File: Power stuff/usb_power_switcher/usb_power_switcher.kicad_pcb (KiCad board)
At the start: 2 copper layers, 36.2 x 17.8 mm, 18 parts, among them J1 IN, J2 Conn_01x04, J3 OUT, J4 D+, J5 D-, J6 USB_OTG, Q1 Q_NPN_BEC, Q2 Q_PMOS_GSD

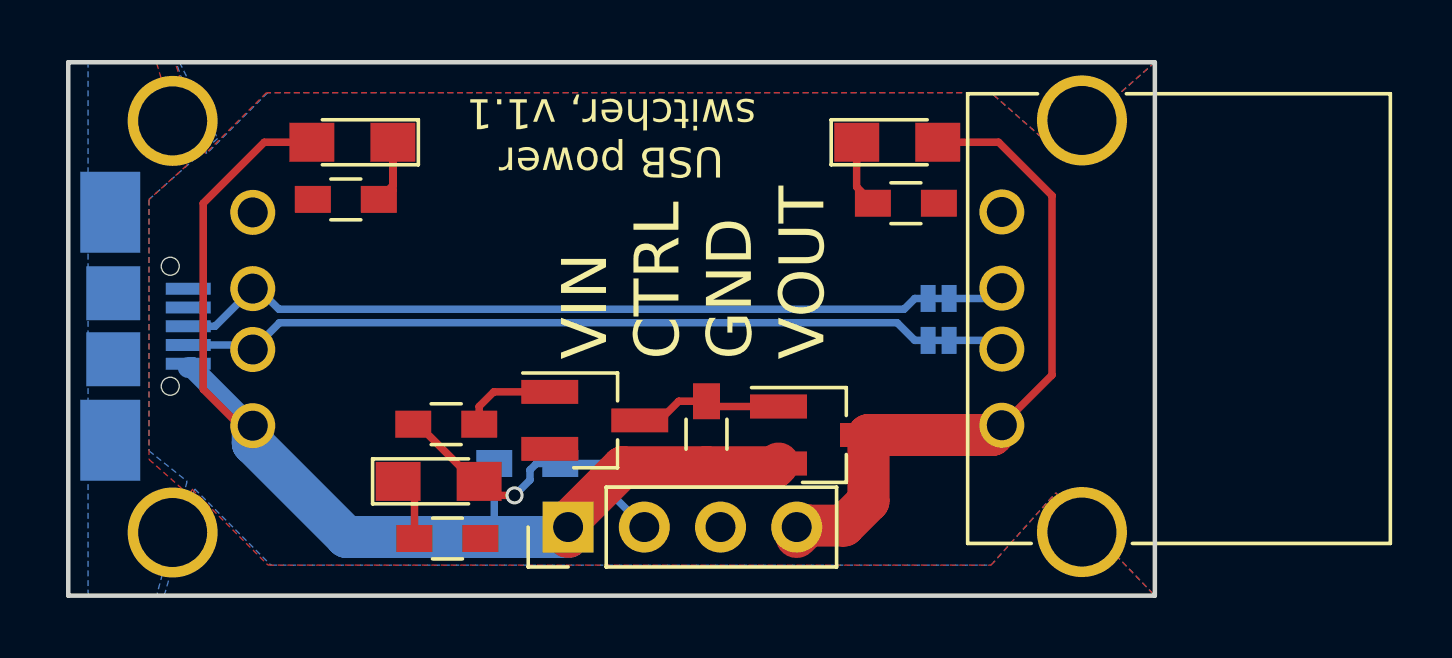
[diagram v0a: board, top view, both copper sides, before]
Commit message: Moving the MicroUSB socket to the top layer so that the board is easier to assemble, rearranging silkscreen a bit
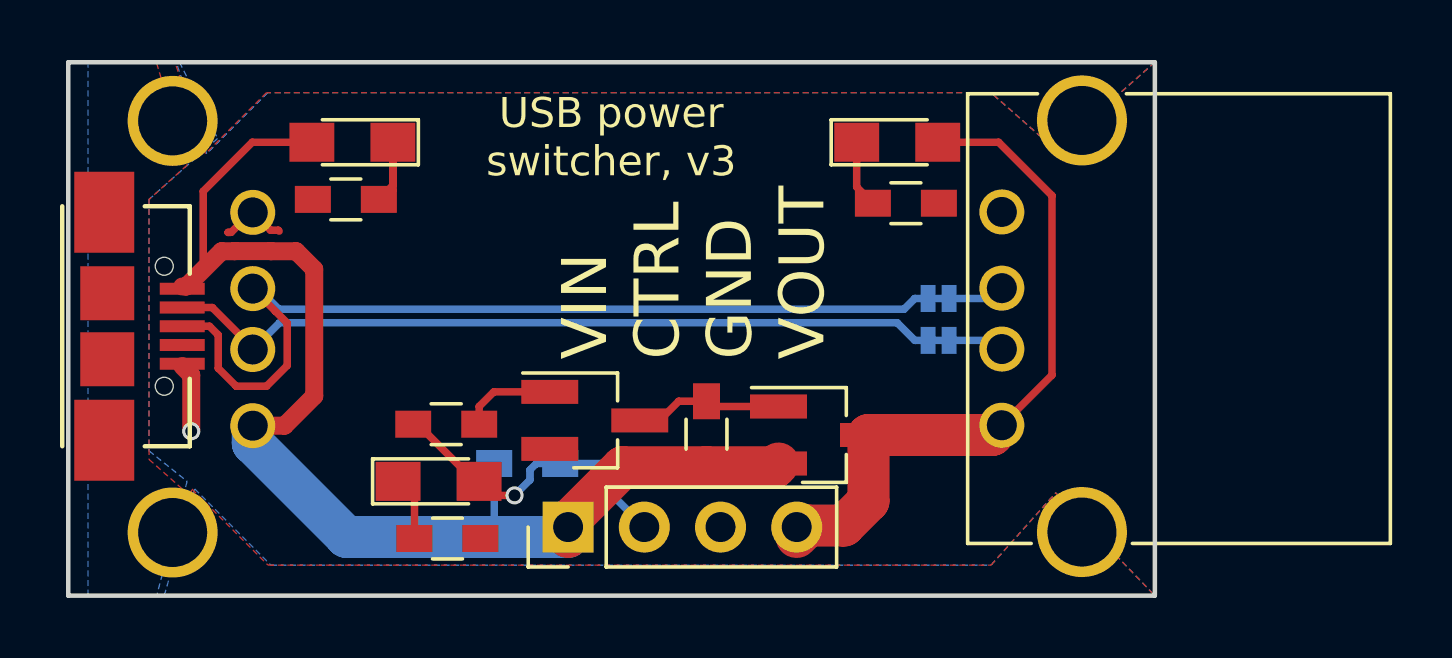
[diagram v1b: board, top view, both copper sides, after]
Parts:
- J6: moved to F.Cu
- moved J6 0.20 mm to (127.6, 97.7), turned to 90 degrees
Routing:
- net D+: track 28.4 -> 34.0 mm
- net GND: track 0.00 -> 4.54 mm, vias 0 -> 1
- net +5V: track 39.6 -> 43.9 mm
- net D-: track 27.9 -> 28.9 mm
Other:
- board text added: "USB power switcher, v3"
- board text removed: "USB power switcher, v1.1"

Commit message: Reloading the USB power switcher project files
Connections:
- J6 pad 4: (no net) -> Net-(J6-Pad4)
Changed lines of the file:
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@@
     (zones 0)
     (modules 18)
-    (nets 13)
+    (nets 14)
   )
   (page A4)
@@
   )
   (setup
-    (last_trace_width 0.6)
+    (last_trace_width 0.25)
     (user_trace_width 0.5)
     (user_trace_width 0.6)
@@
   (net 11 "Net-(D3-Pad1)")
   (net 12 "Net-(Q1-Pad3)")
+  (net 13 "Net-(J6-Pad4)")
   (net_class Default "This is the default net class."
     (clearance 0.2)
@@
     (add_net "Net-(D2-Pad1)")
     (add_net "Net-(D3-Pad1)")
+    (add_net "Net-(J6-Pad4)")
     (add_net "Net-(Q1-Pad1)")
     (add_net "Net-(Q1-Pad3)")
@@
     (pad 3 smd rect (at 0 0 90) (size 0.4 1.5) (layers F.Cu F.Paste F.Mask)
       (net 2 D+))
-    (pad 4 smd rect (at -0.625 0 90) (size 0.4 1.5) (layers F.Cu F.Paste F.Mask))
+    (pad 4 smd rect (at -0.625 0 90) (size 0.4 1.5) (layers F.Cu F.Paste F.Mask)
+      (net 13 "Net-(J6-Pad4)"))
     (pad 5 smd rect (at -1.25 0 90) (size 0.4 1.5) (layers F.Cu F.Paste F.Mask)
       (net 1 GND))

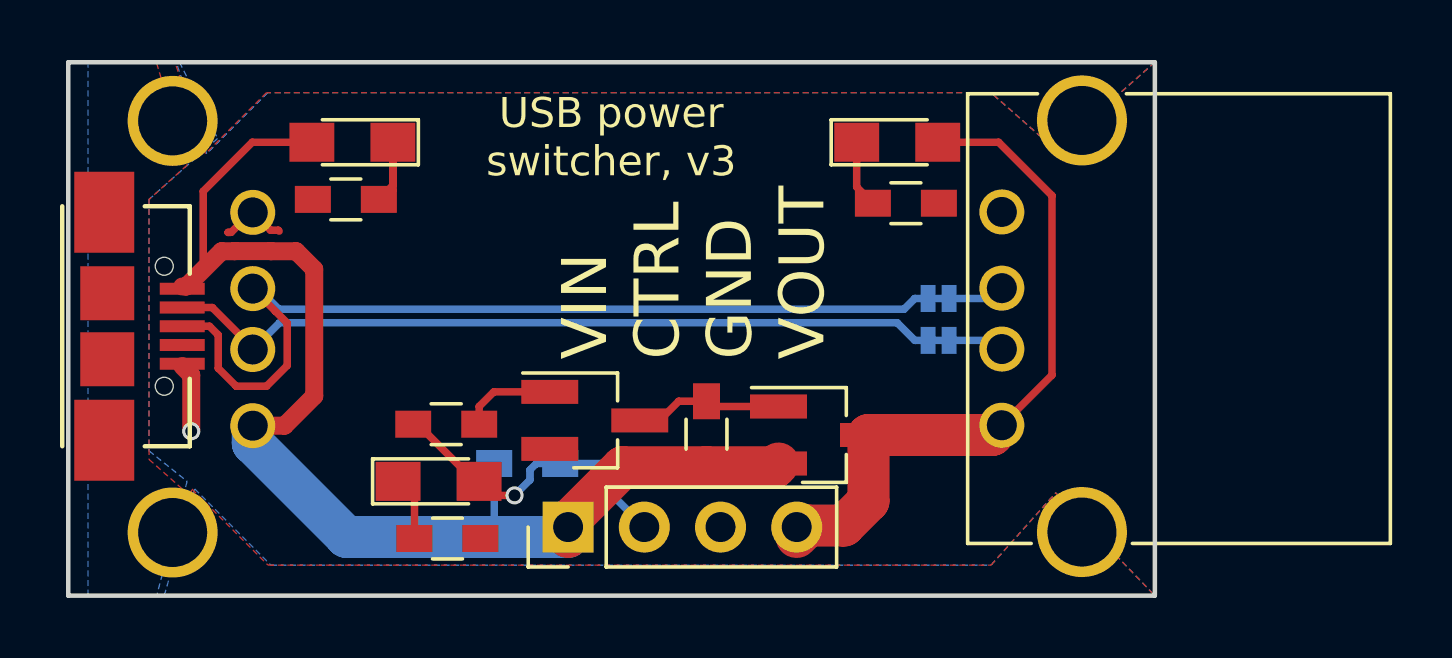
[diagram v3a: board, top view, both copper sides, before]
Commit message: Changing the USB power switcher dimensions to be more reasonable, adding a README
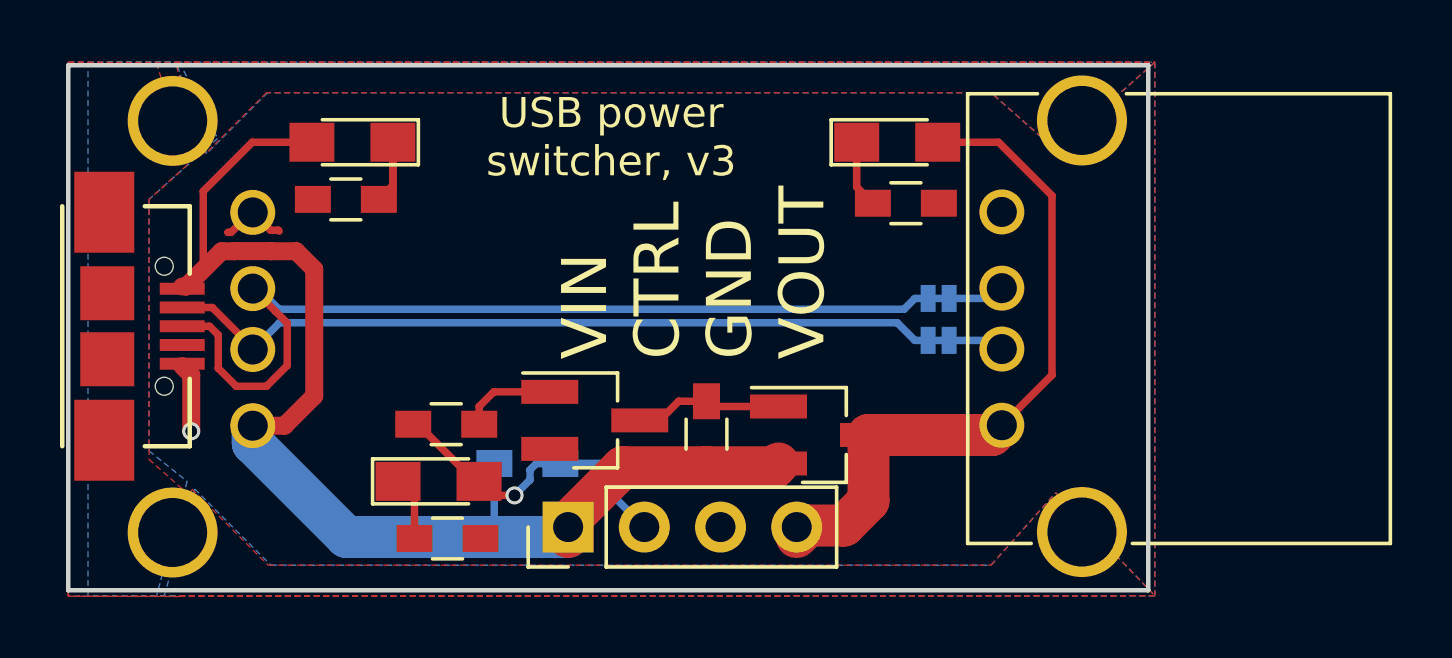
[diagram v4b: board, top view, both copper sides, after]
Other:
- board size 36.2 x 17.8 mm -> 36 x 17.5 mm
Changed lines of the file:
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@@
     (pad_drill 1)
     (pad_to_mask_clearance 0.2)
-    (aux_axis_origin 160 88.9)
+    (aux_axis_origin 159.8 89)
     (visible_elements 7FFFFFFF)
     (pcbplotparams
@@
     (effects (font (size 1.5 1.5) (thickness 0.3)) (justify left mirror))
   )
-  (gr_line (start 160.02 88.9) (end 123.8 88.9) (layer Edge.Cuts) (width 0.15))
-  (gr_line (start 160.02 106.68) (end 160.02 88.9) (layer Edge.Cuts) (width 0.15))
-  (gr_line (start 123.8 106.68) (end 160.02 106.68) (layer Edge.Cuts) (width 0.15))
-  (gr_line (start 123.8 88.9) (end 123.8 106.68) (layer Edge.Cuts) (width 0.15))
+  (gr_line (start 159.8 89) (end 123.8 89) (layer Edge.Cuts) (width 0.15))
+  (gr_line (start 159.8 106.5) (end 159.8 89) (layer Edge.Cuts) (width 0.15))
+  (gr_line (start 123.8 106.5) (end 159.8 106.5) (layer Edge.Cuts) (width 0.15))
+  (gr_line (start 123.8 89) (end 123.8 106.5) (layer Edge.Cuts) (width 0.15))
   (segment (start 129.95 93.905) (end 130.545 94.5) (width 0.25) (layer F.Cu) (net 1))
   (segment (start 130.8 94.5) (end 130.829991 94.529991) (width 0.25) (layer F.Cu) (net 1))
